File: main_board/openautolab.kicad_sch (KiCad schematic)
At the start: 35 parts, among them J1 PIN11, J10 HX711, J11 LCD, J16 PWR_IN, J17 FILTER_PUMP, J18 FILTER_SENSOR, J2 PIN9, J3 PIN10, J4 PIN12, J6 PIN7, J7 PIN8, J8 PUMP, J9 SERVO, K1 FINDER-36.11, K2 FINDER-36.11, SW0 PIN_A0, SW1 PIN_A1, SW2 PIN_A2, SW3 SW_DPST_x2, SW4 SW_DPST_x2, U1 TD62064APG, U2 TD62064APG, U3 LM2576T-5

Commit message: update board
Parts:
- removed BZ0: Buzzer, Buzzer_Beeper:Buzzer_12x9.5RM7.6, symbol Device:Buzzer
- removed D1, D2, D3, D4, D5: 1N4004, Diode_THT:D_DO-41_SOD81_P10.16mm_Horizontal, symbol Diode:1N4004
- removed D6: 1N5822, Diode_THT:D_DO-201AD_P15.24mm_Horizontal, symbol Diode:1N5822
- removed K1, K2: FINDER-36.11, Relay_THT:Relay_SPDT_Finder_36.11, symbol Relay:FINDER-36.11
- removed NT1: NetTie_2, NetTie:NetTie-2_SMD_Pad2.0mm, symbol Device:NetTie_2
- removed U1, U2: TD62064APG, Package_DIP:DIP-16_W7.62mm, symbol Transistor_Array:TD62064APG
- removed U3: LM2576T-5, Package_TO_SOT_THT:TO-220-5_Vertical, symbol Regulator_Switching:LM2576T-5
- added D1, D10, D2, D3, D4, D5, D6, D7, D8: 1N5819WS, Diode_SMD:D_SOD-323, symbol Diode:1N5819WS
- added D9: 1N5819, Diode_SMD:D_SOD-323, symbol Diode:1N5819
- added J5: PIN9, TerminalBlock_Phoenix:TerminalBlock_Phoenix_PT-1,5-2-3.5-H_1x02_P3.50mm_Horizontal, symbol Connector:Screw_Terminal_01x02
- added J9: PUMP, TerminalBlock_Phoenix:TerminalBlock_Phoenix_MKDS-3-2-5.08_1x02_P5.08mm_Horizontal, symbol Connector:Screw_Terminal_01x02
- added Q1, Q2, Q3, Q4, Q5, Q6, Q7, Q8: TSM2302CX, Package_TO_SOT_SMD:SOT-23, symbol Transistor_FET:TSM2302CX
- added R1, R10, R12, R14, R16, R4, R6, R8: 10k, Resistor_SMD:R_0603_1608Metric, symbol Device:R
- added R11, R13, R15, R2, R3, R5, R7, R9: 100, Resistor_SMD:R_0603_1608Metric, symbol Device:R
- added U1: DRV8870DDA, Package_SO:Texas_HTSOP-8-1EP_3.9x4.9mm_P1.27mm_EP2.95x4.9mm_Mask2.4x3.1mm_ThermalVias, symbol Driver_Motor:DRV8870DDA
- added U2: LM2575-5.0BU, Package_TO_SOT_SMD:TO-263-5_TabPin3, symbol Regulator_Switching:LM2575-5.0BU
- C1: value C_Polarized -> 100; footprint Capacitor_THT:CP_Radial_D10.0mm_P5.00mm -> Capacitor_SMD:CP_Elec_6.3x5.4
- C2: value C_Polarized -> 330; footprint Capacitor_THT:CP_Radial_D8.0mm_P5.00mm -> Capacitor_SMD:CP_Elec_8x10
- J1: value PIN11 -> PIN13; footprint TerminalBlock_Phoenix:TerminalBlock_Phoenix_MKDS-3-2-5.08_1x02_P5.08mm_Horizontal -> TerminalBlock_Phoenix:TerminalBlock_Phoenix_PT-1,5-2-3.5-H_1x02_P3.50mm_Horizontal
- J2: value PIN9 -> PIN12; footprint TerminalBlock_Phoenix:TerminalBlock_Phoenix_MKDS-3-2-5.08_1x02_P5.08mm_Horizontal -> TerminalBlock_Phoenix:TerminalBlock_Phoenix_PT-1,5-2-3.5-H_1x02_P3.50mm_Horizontal
- J3: value PIN10 -> PIN11; footprint TerminalBlock_Phoenix:TerminalBlock_Phoenix_MKDS-3-2-5.08_1x02_P5.08mm_Horizontal -> TerminalBlock_Phoenix:TerminalBlock_Phoenix_PT-1,5-2-3.5-H_1x02_P3.50mm_Horizontal
- J4: value PIN12 -> PIN10; footprint TerminalBlock_Phoenix:TerminalBlock_Phoenix_MKDS-3-2-5.08_1x02_P5.08mm_Horizontal -> TerminalBlock_Phoenix:TerminalBlock_Phoenix_PT-1,5-2-3.5-H_1x02_P3.50mm_Horizontal
- J6: value PIN7 -> PIN8; footprint TerminalBlock_Phoenix:TerminalBlock_Phoenix_MKDS-3-2-5.08_1x02_P5.08mm_Horizontal -> TerminalBlock_Phoenix:TerminalBlock_Phoenix_PT-1,5-2-3.5-H_1x02_P3.50mm_Horizontal
- J7: value PIN8 -> PIN7; footprint TerminalBlock_Phoenix:TerminalBlock_Phoenix_MKDS-3-2-5.08_1x02_P5.08mm_Horizontal -> TerminalBlock_Phoenix:TerminalBlock_Phoenix_PT-1,5-2-3.5-H_1x02_P3.50mm_Horizontal
- J8: value PUMP -> PINA0; footprint TerminalBlock_Phoenix:TerminalBlock_Phoenix_MKDS-3-2-5.08_1x02_P5.08mm_Horizontal -> TerminalBlock_Phoenix:TerminalBlock_Phoenix_PT-1,5-2-3.5-H_1x02_P3.50mm_Horizontal
- L1: value L -> 330; footprint Inductor_THT:L_Toroid_Vertical_L26.7mm_W14.0mm_P10.16mm_Pulse_D -> Inductor_SMD:L_12x12mm_H8mm
- SW0, SW1, SW2: footprint Button_Switch_THT:SW_PUSH_6mm -> Button_Switch_SMD:SW_Push_1P1T_NO_6x6mm_H9.5mm
- renumbered J17 to J10, J18 to J11, J16 to J12, J10 to J13, J9 to J14, J11 to J15
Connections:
- net GNDPWR is gone; now on net GND: J11.1 (Pin_1), J12.1 (Pin_1)
- net +12V: now also J8.2 (Pin_2), D1.1 (K), D10.1 (K), D2.1 (K), D3.1 (K), D4.1 (K), D5.1 (K), D6.1 (K), D7.1 (K), D8.1 (K), J5.2 (Pin_2), U1.5 (VM), U2.4 (FB)
- net +5V: now also U1.4 (VREF), U2.1 (VIN)
- net GND: now also D9.2 (A), Q1.2 (S), Q2.2 (S), Q3.2 (S), Q4.2 (S), Q5.2 (S), Q6.2 (S), Q7.2 (S), Q8.2 (S), R1.2, R10.2, R12.2, R14.2, R16.2, R4.2, R6.2, R8.2, U1.1 (GND), U1.7 (ISEN), U1.9 (GND), U2.2 (OUT), U2.3 (GND)
- net at J8.1 (Pin_1): now also D8.2 (A), Q8.3 (D)
- net at J4.1 (Pin_1): now also D4.2 (A), Q4.3 (D)
- net at J3.1 (Pin_1): now also D3.2 (A), Q3.3 (D)
- net at J7.1 (Pin_1): now also D7.2 (A), Q7.3 (D)
- net at SW1.1: now also A1.21 (A2); no longer A1.20 (A1)
- net at J2.1 (Pin_1): now also D2.2 (A), Q2.3 (D)
- net at A1.9 (D6): now also R5.1
- net at A1.11 (D8): now also R9.1
- net at J6.1 (Pin_1): now also D6.2 (A), Q6.3 (D)
- net at A1.10 (D7): now also R7.1
- net at A1.8 (D5): now also R3.1
- net at L1.1: now also D9.1 (K), U2.5 (~{ON}/OFF)
- net at A1.13 (D10): now also R13.1
- net at A1.15 (D12): now also U1.2 (IN2)
- net at J1.1 (Pin_1): now also D1.2 (A), Q1.3 (D)
- net at A1.14 (D11): now also R15.1
- net at A1.12 (D9): now also R11.1
- net at J10.1 (Pin_1), SW3.1 (A): now also D10.2 (A)
- net at A1.19 (A0): now also R2.1; no longer SW0.1
- net at SW2.1: now also A1.20 (A1); no longer A1.21 (A2)
- net at A1.16 (D13): now also U1.3 (IN1)
- net at A1.22 (A3): now also SW0.1
- new net: Q6.1 (G), R11.2, R12.1
- new net: J9.1 (Pin_1), U1.8 (OUT2)
- new net: J9.2 (Pin_2), U1.6 (OUT1)
- new net: D5.2 (A), J5.1 (Pin_1), Q5.3 (D)
- new net: Q8.1 (G), R15.2, R16.1
- new net: Q5.1 (G), R10.1, R9.2
- new net: Q1.1 (G), R1.1, R2.2
- new net: Q3.1 (G), R5.2, R6.1
- new net: Q7.1 (G), R13.2, R14.1
- new net: Q4.1 (G), R7.2, R8.1
- new net: Q2.1 (G), R3.2, R4.1
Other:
- moved on the sheet: A1, C1, C2, J1, J10, J11, J12, J13, J14, J15, L1, SW0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

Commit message: update schematic, complete parts description
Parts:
- removed D1, D2, D3, D4, D5, D6, D7, D8: 1N5819WS, Diode_SMD:D_SOD-323, symbol Diode:1N5819WS
- removed D9: 1N5819, Diode_SMD:D_SOD-323, symbol Diode:1N5819
- removed Q1, Q2, Q3, Q4, Q5, Q6, Q7, Q8: TSM2302CX, Package_TO_SOT_SMD:SOT-23, symbol Transistor_FET:TSM2302CX
- removed R1, R10, R12, R14, R16, R4, R6, R8: 10k, Resistor_SMD:R_0603_1608Metric, symbol Device:R
- removed R11, R13, R15, R2, R3, R5, R7, R9: 100, Resistor_SMD:R_0603_1608Metric, symbol Device:R
- removed U1: DRV8870DDA, Package_SO:Texas_HTSOP-8-1EP_3.9x4.9mm_P1.27mm_EP2.95x4.9mm_Mask2.4x3.1mm_ThermalVias, symbol Driver_Motor:DRV8870DDA
- removed U2: LM2575-5.0BU, Package_TO_SOT_SMD:TO-263-5_TabPin3, symbol Regulator_Switching:LM2575-5.0BU
- added D1: 1N5819WS, Diode_THT:D_A-405_P7.62mm_Horizontal, symbol Device:D_Schottky
- added IC1, IC3: ULN2065B, Package_DIP:DIP-16_W7.62mm, symbol ULN2065B:ULN2065B
- added U1: ~, Pololu_breakout_DRV8874:Pololu_breakout_DRV8874, symbol Pololu_breakout_DRV8874:Pololu_breakout_DRV8874
- added U2: LM2575-5.0BT, Package_TO_SOT_THT:TO-220-5_P3.4x3.7mm_StaggerOdd_Lead3.8mm_Vertical, symbol Regulator_Switching:LM2575-5.0BT
- C1: footprint Capacitor_SMD:CP_Elec_6.3x5.4 -> Capacitor_THT:CP_Radial_D8.0mm_P5.00mm
- C2: footprint Capacitor_SMD:CP_Elec_8x10 -> Capacitor_THT:CP_Radial_D8.0mm_P5.00mm
- D10: footprint Diode_SMD:D_SOD-323 -> Diode_THT:D_A-405_P7.62mm_Horizontal; symbol Diode:1N5819WS -> Device:D_Schottky
- J1: value PIN13 -> PIN11
- J2: value PIN12 -> PIN10
- J3: value PIN11 -> PIN9
- J4: value PIN10 -> PIN8
- J5: value PIN9 -> PIN7
- J6: value PIN8 -> PIN6
- J7: value PIN7 -> PIN5
- L1: footprint Inductor_SMD:L_12x12mm_H8mm -> Inductor_THT:L_Radial_D12.0mm_P5.00mm_Fastron_11P
- SW0, SW1, SW2: footprint Button_Switch_SMD:SW_Push_1P1T_NO_6x6mm_H9.5mm -> Button_Switch_THT:SW_PUSH_6mm
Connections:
- net +12V: now also IC1.1 (K1), IC1.8 (K2), IC3.1 (K1), IC3.8 (K2), U1.14 (VIN), U2.4 (FB)
- net +5V: now also U1.5 (PMODE), U1.6 (SLEEP), U2.1 (VIN)
- net GND: now also J11.2 (Pin_2), D1.2 (A), IC1.12 (GND@3), IC1.13 (GND@4), IC1.4 (GND@1), IC1.5 (GND@2), IC3.12 (GND@3), IC3.13 (GND@4), IC3.4 (GND@1), IC3.5 (GND@2), U1.13 (GND_PWR), U1.2 (GND), U2.2 (OUT), U2.3 (GND); no longer A1.4 (GND), J11.1 (Pin_1)
- net at J6.1 (Pin_1): now also IC1.7 (O2)
- net at J9.1 (Pin_1): now also U1.12 (OUT2)
- net at J9.2 (Pin_2): now also U1.11 (OUT1)
- net at J4.1 (Pin_1): now also IC3.16 (O4)
- net at J5.1 (Pin_1): now also IC1.2 (O1)
- net at J8.1 (Pin_1): now also IC1.16 (O4)
- net at A1.11 (D8): now also IC3.3 (I1)
- net at A1.19 (A0): now also IC1.14 (I4)
- net at SW3.2 (B): now also J11.1 (Pin_1); no longer J11.2 (Pin_2)
- net at A1.13 (D10): now also IC3.11 (I3)
- net at J3.1 (Pin_1): now also IC3.9 (O3)
- net at A1.14 (D11): now also IC3.14 (I4)
- net at J1.1 (Pin_1): now also IC3.2 (O1)
- net at J2.1 (Pin_1): now also IC3.7 (O2)
- net at J7.1 (Pin_1): now also IC1.9 (O3)
- net at A1.10 (D7): now also IC1.3 (I1)
- net at A1.12 (D9): now also IC3.6 (I2)
- net at A1.15 (D12): now also U1.3 (EN/IN1)
- net at A1.16 (D13): now also U1.4 (PH/IN2)
- net at A1.8 (D5): now also IC1.11 (I3)
- net at A1.9 (D6): now also IC1.6 (I2)
- net at L1.1: now also D1.1 (K), U2.5 (~{ON}/OFF)
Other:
- moved on the sheet: A1, C1, C2, D10, J10, J11, J12, J13, J14, J15, J9, L1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

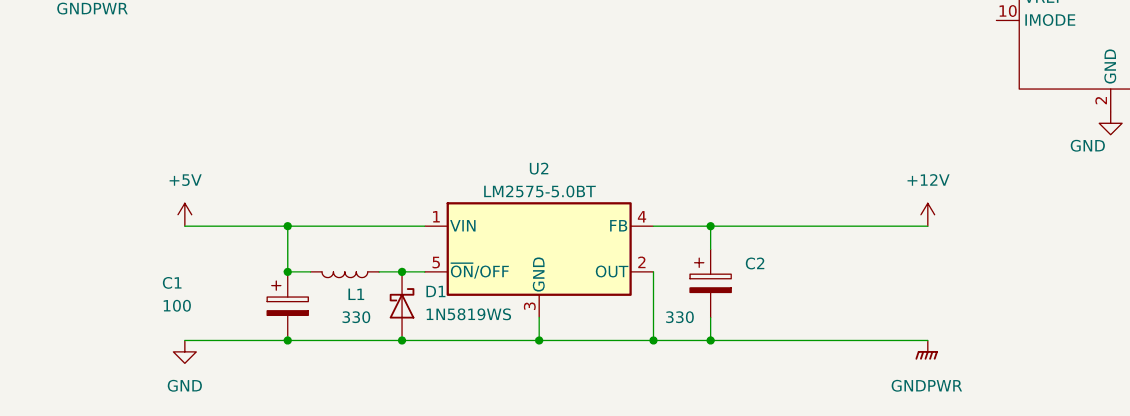
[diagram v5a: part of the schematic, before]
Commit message: fixed error in board
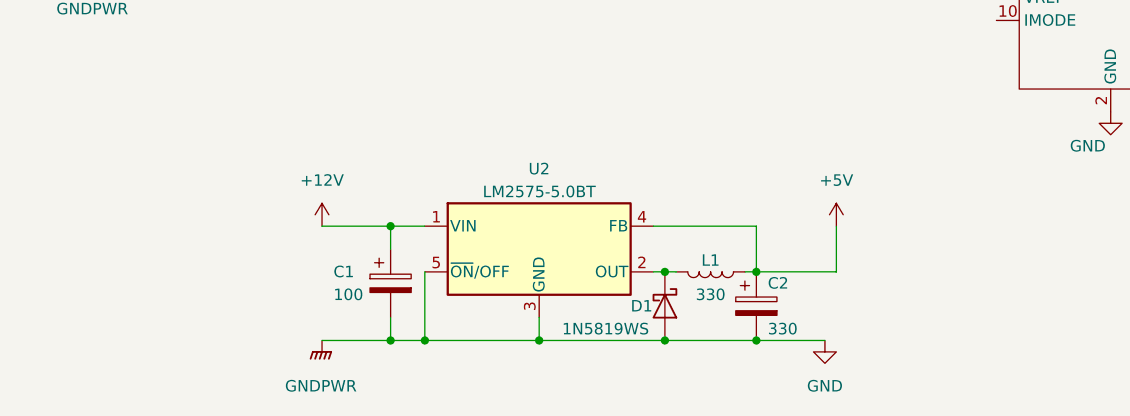
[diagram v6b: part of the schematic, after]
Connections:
- net +12V: now also C1.1, U2.1 (VIN); no longer C2.1, U2.4 (FB)
- net +5V: now also C2.1, L1.1, U2.4 (FB); no longer C1.1, L1.2, U2.1 (VIN)
- net GND: now also U2.5 (~{ON}/OFF); no longer U2.2 (OUT)
- new net: D1.1 (K), L1.2, U2.2 (OUT)
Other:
- moved on the sheet: C1, C2, D1, L1

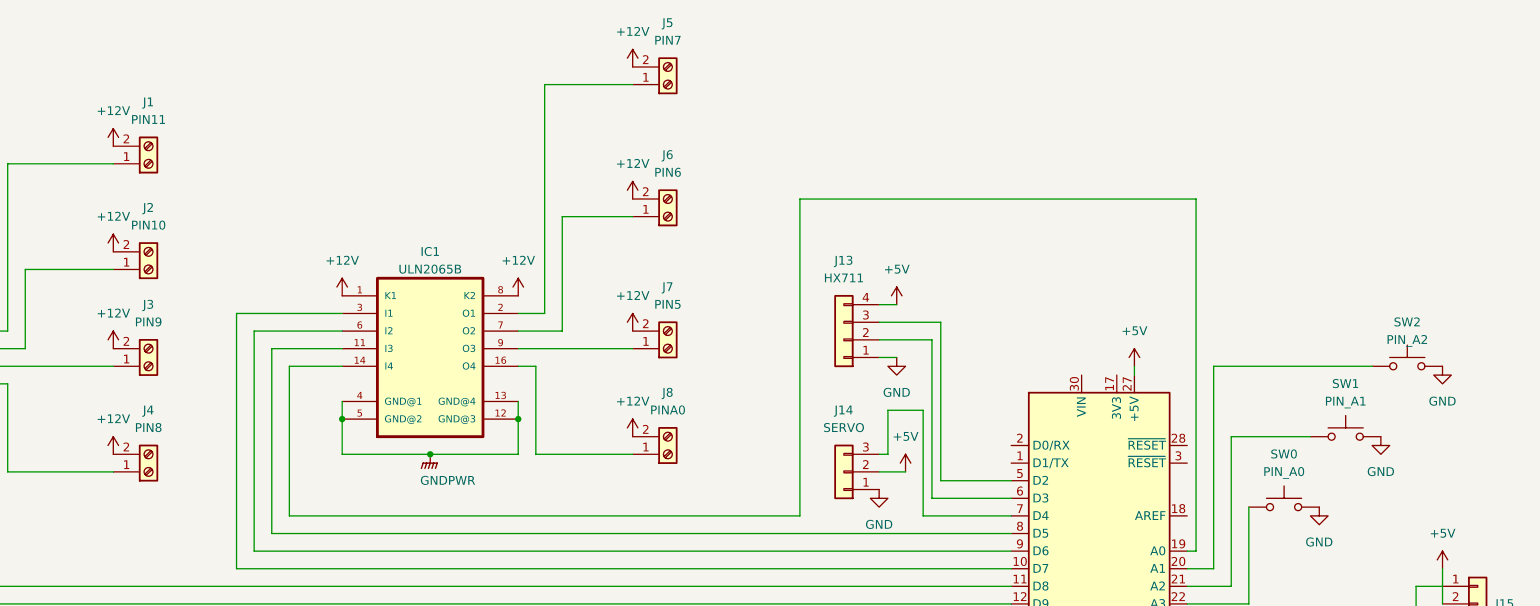
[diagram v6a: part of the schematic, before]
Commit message: more accessible valves, small changes in enclosure
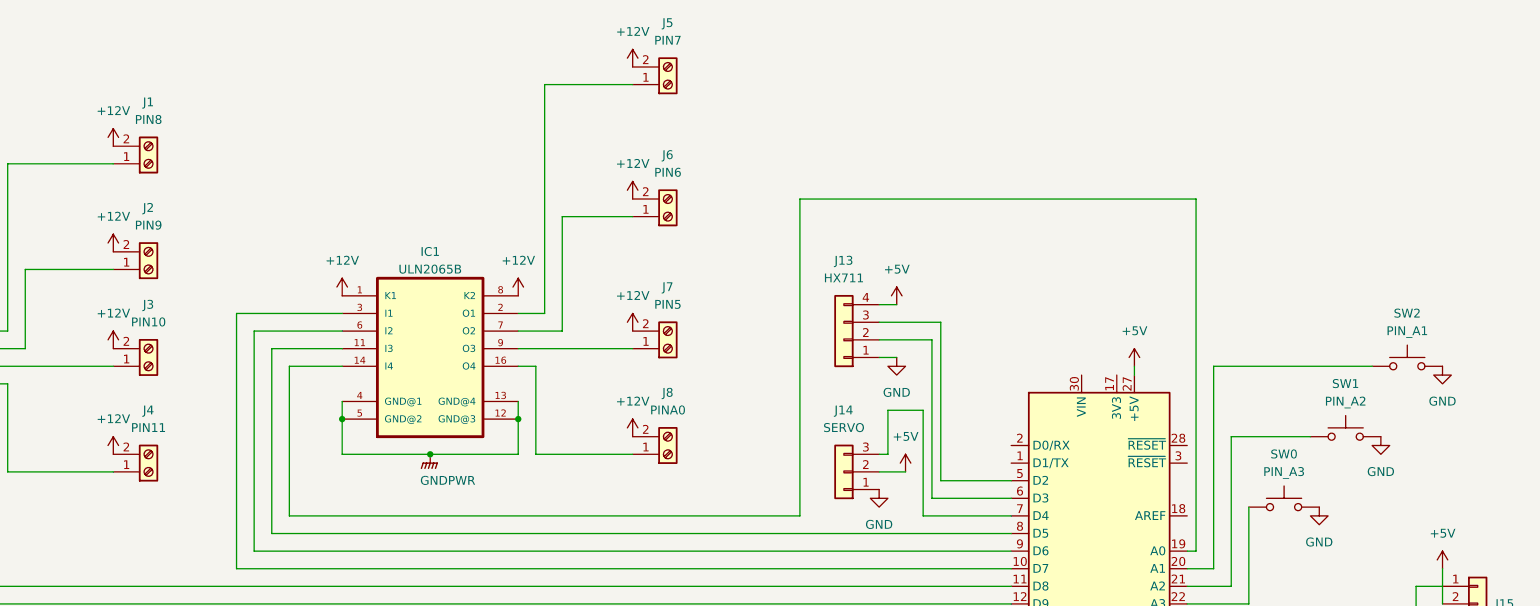
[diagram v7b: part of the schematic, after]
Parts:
- J1: value PIN11 -> PIN8
- J2: value PIN10 -> PIN9
- J3: value PIN9 -> PIN10
- J4: value PIN8 -> PIN11
- SW0: value PIN_A0 -> PIN_A3
- SW1: value PIN_A1 -> PIN_A2
- SW2: value PIN_A2 -> PIN_A1
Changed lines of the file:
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@@
       (effects (font (size 1.27 1.27)))
     )
-    (property "Value" "PIN_A1" (at 255.27 72.39 0)
+    (property "Value" "PIN_A2" (at 255.27 72.39 0)
       (effects (font (size 1.27 1.27)))
     )
@@
       (effects (font (size 1.27 1.27)))
     )
-    (property "Value" "PIN9" (at 82.55 60.96 0)
+    (property "Value" "PIN10" (at 82.55 60.96 0)
       (effects (font (size 1.27 1.27)))
     )
@@
       (effects (font (size 1.27 1.27)))
     )
-    (property "Value" "PIN8" (at 82.55 76.2 0)
+    (property "Value" "PIN11" (at 82.55 76.2 0)
       (effects (font (size 1.27 1.27)))
     )
@@
       (effects (font (size 1.27 1.27)))
     )
-    (property "Value" "PIN10" (at 82.55 46.99 0)
+    (property "Value" "PIN9" (at 82.55 46.99 0)
       (effects (font (size 1.27 1.27)))
     )
@@
       (effects (font (size 1.27 1.27)))
     )
-    (property "Value" "PIN11" (at 82.55 31.75 0)
+    (property "Value" "PIN8" (at 82.55 31.75 0)
       (effects (font (size 1.27 1.27)))
     )
@@
       (effects (font (size 1.27 1.27)))
     )
-    (property "Value" "PIN_A0" (at 246.38 82.55 0)
+    (property "Value" "PIN_A3" (at 246.38 82.55 0)
       (effects (font (size 1.27 1.27)))
     )
@@
   (symbol (lib_id "Switch:SW_Push") (at 264.16 67.31 0) (unit 1)
     (in_bom yes) (on_board yes) (dnp no) (fields_autoplaced)
-    (property "Reference" "SW2" (at 264.16 60.96 0)
-      (effects (font (size 1.27 1.27)))
-    )
-    (property "Value" "PIN_A2" (at 264.16 63.5 0)
-      (effects (font (size 1.27 1.27)))
-    )
+    (property "Reference" "SW2" (at 264.16 59.69 0)
+      (effects (font (size 1.27 1.27)))
+    )
+    (property "Value" "PIN_A1" (at 264.16 62.23 0)
+      (effects (font (size 1.27 1.27)))
+    )
